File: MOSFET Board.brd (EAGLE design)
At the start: 58.4 x 104.1 mm, 36 parts, among them J1 POWERPOLE_POWER25A, J2 POWERPOLE_POWER25A, J3 POWERPOLE_POWER25A, J4 POWERPOLE_POWER25A, J5 POWERPOLE_POWER25A, J6 POWERPOLE_POWER25A, J7 POWERPOLE_POWER25A, J8 POWERPOLE_POWER25A, J9 POWERPOLE_POWER25A, Q1 STP55NF06L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

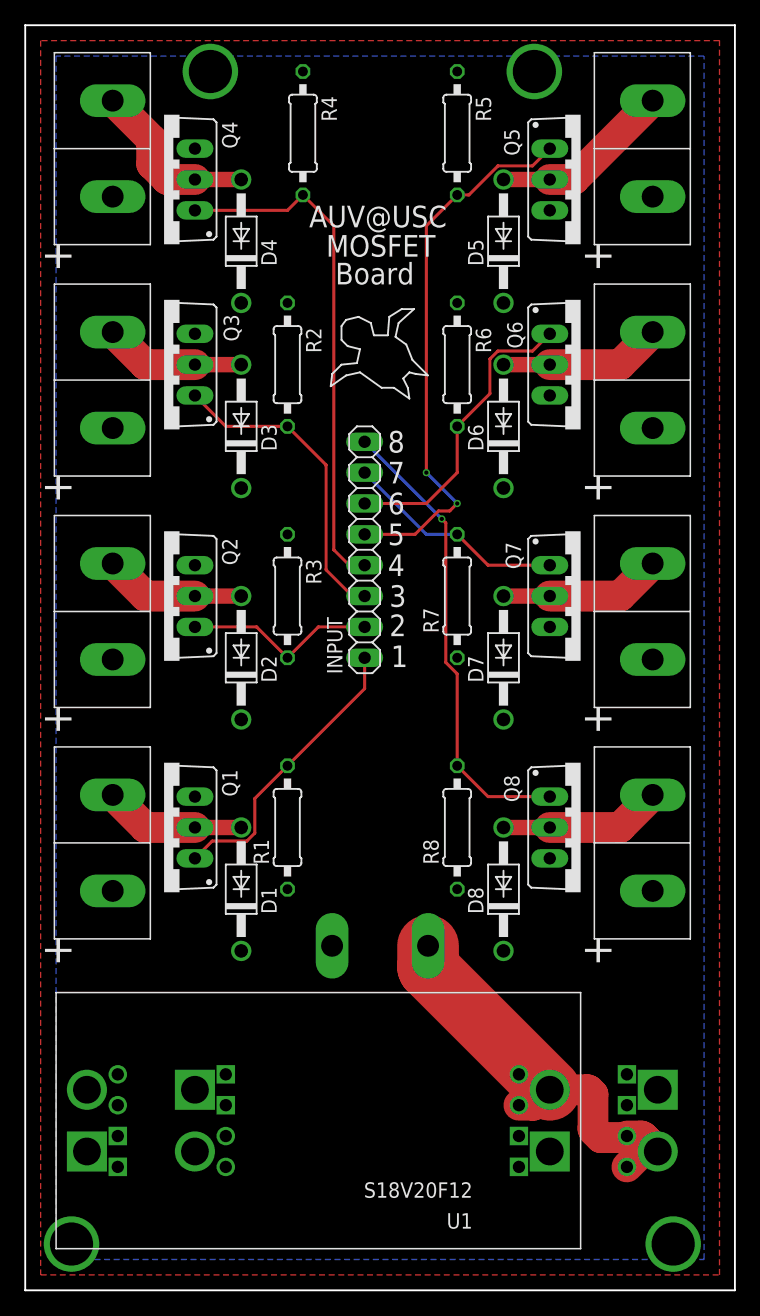
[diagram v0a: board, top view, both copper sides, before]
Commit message: Add numbers to outputs on silkscreen
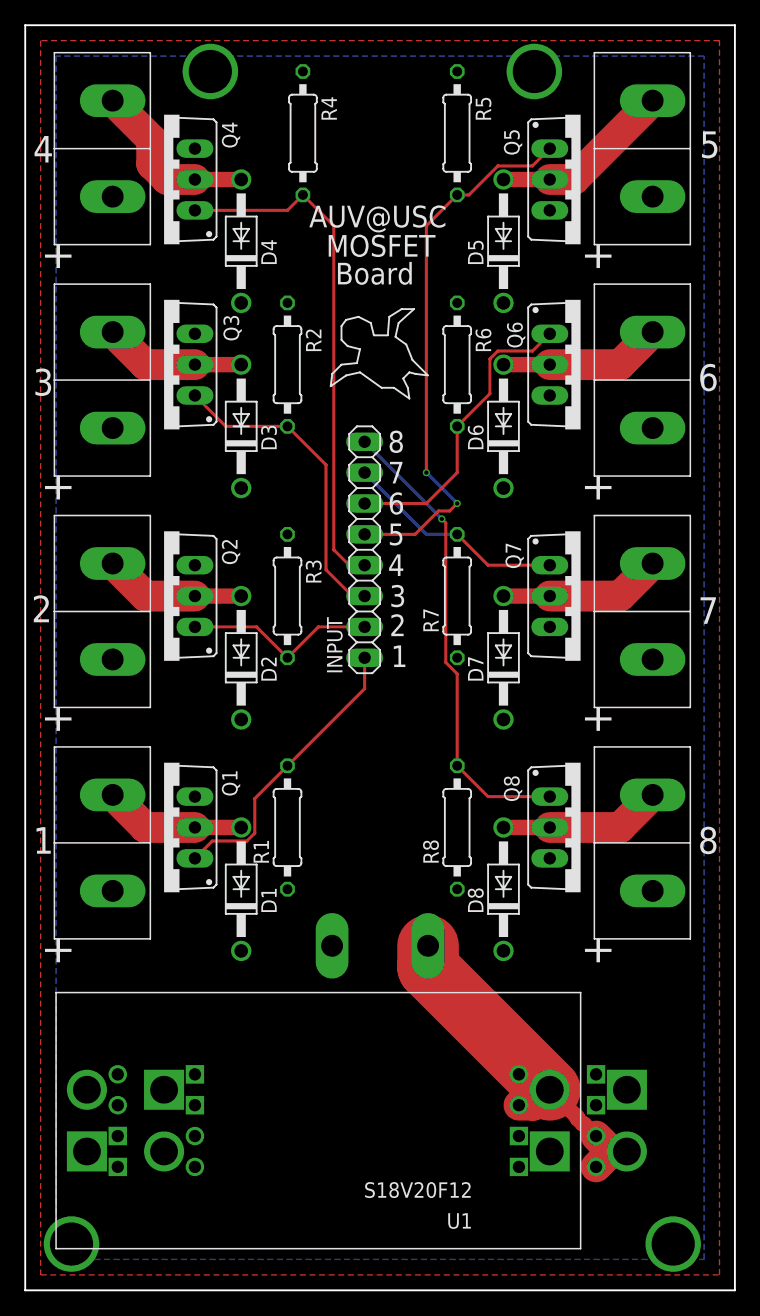
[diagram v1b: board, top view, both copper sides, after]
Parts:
- moved U$1 2.54 mm to (30.5, 12.7)
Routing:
- net VIN: track 40.8 -> 32.4 mm
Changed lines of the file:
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@@
 <text x="29.845" y="67.691" size="1.778" layer="21">8</text>
 <text x="55.88" y="99.06" size="1.778" layer="22" rot="MR0">Rev. 1</text>
+<text x="0.508" y="53.721" size="2.1844" layer="21">2</text>
+<text x="0.635" y="34.671" size="2.1844" layer="21">1</text>
+<text x="0.635" y="72.39" size="2.1844" layer="21">3</text>
+<text x="0.635" y="91.567" size="2.1844" layer="21">4</text>
+<text x="55.499" y="91.948" size="2.1844" layer="21">5</text>
+<text x="55.372" y="72.771" size="2.1844" layer="21">6</text>
+<text x="55.372" y="53.594" size="2.1844" layer="21">7</text>
+<text x="55.372" y="34.671" size="2.1844" layer="21">8</text>
+<dimension x1="0" y1="105.41" x2="58.42" y2="105.41" x3="29.21" y3="107.95" textsize="2.1844" layer="21"/>
+<dimension x1="59.69" y1="102.87" x2="59.69" y2="-1.27" x3="63.5" y3="50.8" textsize="2.1844" layer="21"/>
 </plain>
 <attributes>
@@
 <element name="R8" library="resistor" library_urn="urn:adsk.eagle:library:348" package="0207/10" package3d_urn="urn:adsk.eagle:package:25939/1" value="2.2k" x="35.56" y="36.83" rot="R90"/>
 <element name="U1" library="custom" package="S18V20" value="S18V20F12" x="24.13" y="12.7" rot="R180"/>
-<element name="U$1" library="custom" package="S18V20" value="S18V20F12" x="33.02" y="12.7" rot="MR0"/>
+<element name="U$1" library="custom" package="S18V20" value="S18V20F12" x="30.48" y="12.7" rot="MR0"/>
 </elements>
 <signals>
@@
 <contactref element="U$1" pad="VIN@2"/>
 <contactref element="U$1" pad="VIN@3"/>
-<wire x1="52.07" y1="10.16" x2="51.00139375" y2="11.22860625" width="2.54" layer="1"/>
-<wire x1="51.00139375" y1="11.22860625" x2="50.821790625" y2="11.303" width="2.54" layer="1" curve="44.999295"/>
-<wire x1="50.821790625" y1="11.303" x2="47.371" y2="11.303" width="2.54" layer="1"/>
-<wire x1="47.371" y1="11.303" x2="46.81039375" y2="11.86360625" width="2.54" layer="1"/>
-<wire x1="46.81039375" y1="11.86360625" x2="46.736" y2="12.043209375" width="2.54" layer="1" curve="-44.999295"/>
-<wire x1="46.736" y1="12.043209375" x2="46.736" y2="14.859" width="2.54" layer="1"/>
-<wire x1="46.736" y1="14.859" x2="46.42939375" y2="15.16560625" width="2.54" layer="1"/>
-<wire x1="46.42939375" y1="15.16560625" x2="46.249790625" y2="15.24" width="2.54" layer="1" curve="44.999295"/>
-<wire x1="46.249790625" y1="15.24" x2="43.18" y2="15.24" width="2.54" layer="1"/>
-<wire x1="52.07" y1="10.16" x2="50.905209375" y2="10.16" width="2.54" layer="1"/>
-<wire x1="50.905209375" y1="10.16" x2="50.72560625" y2="10.08560625" width="2.54" layer="1" curve="44.999502"/>
-<wire x1="50.72560625" y1="10.08560625" x2="49.53" y2="8.89" width="2.54" layer="1"/>
-<wire x1="49.53" y1="11.43" x2="50.694790625" y2="11.43" width="2.54" layer="1"/>
-<wire x1="50.694790625" y1="11.43" x2="50.87439375" y2="11.35560625" width="2.54" layer="1" curve="-44.999502"/>
-<wire x1="50.87439375" y1="11.35560625" x2="52.07" y2="10.16" width="2.54" layer="1"/>
 <wire x1="43.18" y1="15.24" x2="33.23439375" y2="25.18560625" width="5.08" layer="1"/>
 <wire x1="33.23439375" y1="25.18560625" x2="33.16" y2="25.365209375" width="5.08" layer="1" curve="-44.999295"/>
@@
 <wire x1="41.83560625" y1="15.31439375" x2="42.015209375" y2="15.24" width="2.54" layer="1" curve="44.999295"/>
 <wire x1="42.015209375" y1="15.24" x2="43.18" y2="15.24" width="2.54" layer="1"/>
+<wire x1="48.26" y1="10.16" x2="46.99" y2="8.89" width="2.54" layer="1"/>
+<wire x1="49.53" y1="10.16" x2="48.26" y2="10.16" width="2.54" layer="1"/>
+<wire x1="48.26" y1="10.16" x2="46.99" y2="11.43" width="2.54" layer="1"/>
+<wire x1="43.18" y1="15.24" x2="45.4406" y2="12.9794" width="1.27" layer="1"/>
+<wire x1="45.4406" y1="12.9794" x2="45.4406" y2="12.88185" width="1.27" layer="1"/>
+<wire x1="45.4406" y1="12.88185" x2="45.90185" y2="12.4206" width="1.27" layer="1"/>
+<wire x1="45.90185" y1="12.4206" x2="45.9994" y2="12.4206" width="1.27" layer="1"/>
+<wire x1="45.9994" y1="12.4206" x2="46.99" y2="11.43" width="1.27" layer="1"/>
 </signal>
 </signals>
